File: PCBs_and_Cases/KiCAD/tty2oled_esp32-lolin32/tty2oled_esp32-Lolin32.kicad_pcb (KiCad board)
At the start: 2 copper layers, 35.6 x 99.7 mm, 12 parts

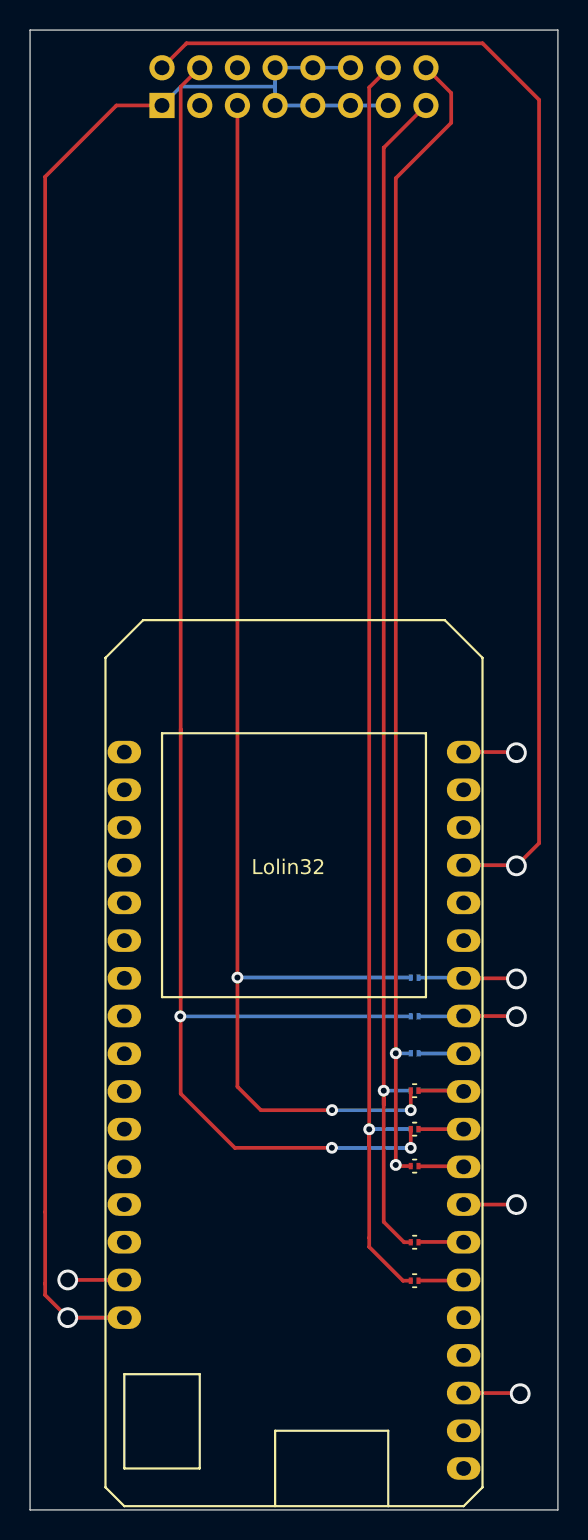
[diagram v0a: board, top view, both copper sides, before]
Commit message: Silkscreen fixed
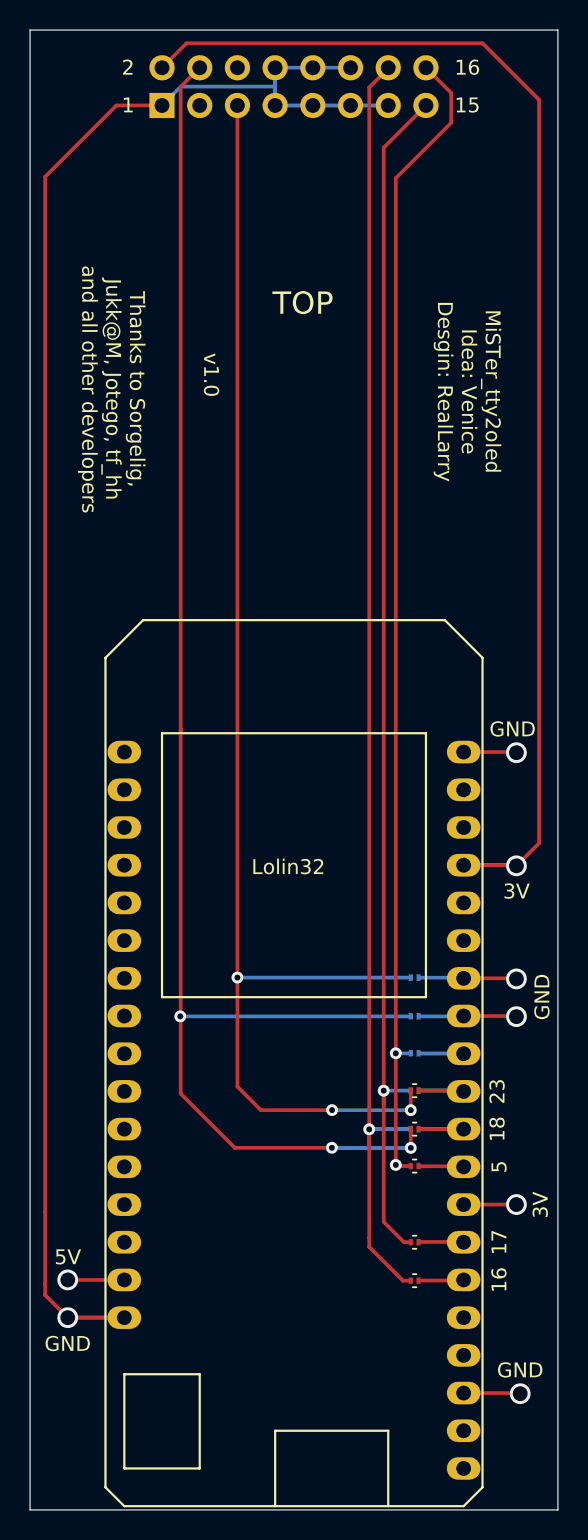
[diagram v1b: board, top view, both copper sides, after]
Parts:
- removed the REF** at (158.0, 122.9) (x2)
- added REF**: R_0201, Resistors_SMD:R_0201, B.Cu at (158.0, 122.9)
- added REF**: R_0201, Resistors_SMD:R_0201, F.Cu at (158.0, 122.9)
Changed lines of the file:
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@@
     )
   )
-  (gr_text v1.0 (at 144.272 74.676 -90) (layer F.Paste)
+  (gr_text v1.0 (at 144.272 74.676 -90) (layer F.SilkS)
     (effects (font (size 1 1) (thickness 0.15)))
   )
-  (gr_text "Thanks to Sorgelig,\nJukk@M, Jotego, tf_hh\nand all other developers" (at 137.668 75.6412 -90) (layer F.Paste)
+  (gr_text "Thanks to Sorgelig,\nJukk@M, Jotego, tf_hh\nand all other developers" (at 137.668 75.6412 -90) (layer F.SilkS)
     (effects (font (size 1 1) (thickness 0.15)))
   )
-  (gr_text "MiSTer_tty2oled\nIdea: Venice\nDesgin: RealLarry" (at 161.6329 75.7809 -90) (layer F.Paste)
+  (gr_text "MiSTer_tty2oled\nIdea: Venice\nDesgin: RealLarry" (at 161.6329 75.7809 -90) (layer F.SilkS)
     (effects (font (size 1 1) (thickness 0.15)))
   )
-  (gr_text 3V (at 166.4843 130.5941 90) (layer F.Paste)
+  (gr_text 3V (at 166.4843 130.5941 90) (layer F.SilkS)
     (effects (font (size 1 1) (thickness 0.15)))
   )
-  (gr_text 3V (at 164.846 109.474) (layer B.Paste)
+  (gr_text 3V (at 164.846 109.474) (layer B.SilkS)
     (effects (font (size 1 1) (thickness 0.15)) (justify mirror))
   )
-  (gr_text GND (at 134.62 139.954) (layer B.Paste)
+  (gr_text GND (at 134.62 139.954) (layer B.SilkS)
     (effects (font (size 1 1) (thickness 0.15)) (justify mirror))
   )
-  (gr_text 3V (at 164.846 109.474) (layer F.Paste)
+  (gr_text 3V (at 164.846 109.474) (layer F.SilkS)
     (effects (font (size 1 1) (thickness 0.15)))
   )
-  (gr_text GND (at 164.592 98.552) (layer F.Paste)
+  (gr_text GND (at 164.592 98.552) (layer F.SilkS)
     (effects (font (size 1 1) (thickness 0.15)))
   )
-  (gr_text GND (at 166.5986 116.5733 90) (layer F.Paste)
+  (gr_text GND (at 166.5986 116.5733 90) (layer F.SilkS)
     (effects (font (size 1 1) (thickness 0.15)))
   )
-  (gr_text GND (at 165.1 141.732) (layer F.Paste)
+  (gr_text GND (at 165.1 141.732) (layer F.SilkS)
     (effects (font (size 1 1) (thickness 0.15)))
   )
-  (gr_text GND (at 134.62 139.954) (layer F.Paste)
+  (gr_text GND (at 134.62 139.954) (layer F.SilkS)
     (effects (font (size 1 1) (thickness 0.15)))
   )
-  (gr_text 5V (at 134.62 134.112) (layer F.Paste)
+  (gr_text 5V (at 134.62 134.112) (layer F.SilkS)
     (effects (font (size 1 1) (thickness 0.15)))
   )
   (gr_line (start 167.64 51.435) (end 132.08 51.435) (layer Edge.Cuts) (width 0.05))
-  (gr_text BOT (at 150.5077 69.7992) (layer B.Paste)
+  (gr_text BOT (at 150.5077 69.7992) (layer B.SilkS)
     (effects (font (size 1.5 1.5) (thickness 0.3)) (justify mirror))
   )
-  (gr_text TOP (at 150.4696 69.85) (layer F.Paste)
+  (gr_text TOP (at 150.4696 69.85) (layer F.SilkS)
     (effects (font (size 1.5 1.5) (thickness 0.3)))
   )
-  (gr_text 16 (at 163.449 125.476 90) (layer B.Paste)
+  (gr_text 16 (at 163.449 125.476 90) (layer B.SilkS)
     (effects (font (size 1 1) (thickness 0.15)) (justify mirror))
   )
-  (gr_text 17 (at 163.449 122.936 90) (layer B.Paste)
+  (gr_text 17 (at 163.449 122.936 90) (layer B.SilkS)
     (effects (font (size 1 1) (thickness 0.15)) (justify mirror))
   )
-  (gr_text 16 (at 163.703 135.636 90) (layer F.Paste)
+  (gr_text 16 (at 163.703 135.636 90) (layer F.SilkS)
     (effects (font (size 1 1) (thickness 0.15)))
   )
-  (gr_text 17 (at 163.703 133.096 90) (layer F.Paste)
+  (gr_text 17 (at 163.703 133.096 90) (layer F.SilkS)
     (effects (font (size 1 1) (thickness 0.15)))
   )
-  (gr_text 5 (at 163.703 128.016 90) (layer F.Paste)
+  (gr_text 5 (at 163.703 128.016 90) (layer F.SilkS)
     (effects (font (size 1 1) (thickness 0.15)))
   )
-  (gr_text 18 (at 163.576 125.476 90) (layer F.Paste)
+  (gr_text 18 (at 163.576 125.476 90) (layer F.SilkS)
     (effects (font (size 1 1) (thickness 0.15)))
   )
-  (gr_text 23 (at 163.576 122.936 90) (layer F.Paste)
+  (gr_text 23 (at 163.576 122.936 90) (layer F.SilkS)
     (effects (font (size 1 1) (thickness 0.15)))
   )
-  (gr_text 5 (at 163.449 120.269 90) (layer B.Paste)
+  (gr_text 5 (at 163.449 120.269 90) (layer B.SilkS)
     (effects (font (size 1 1) (thickness 0.15)) (justify mirror))
   )
-  (gr_text 18 (at 163.449 117.856 90) (layer B.Paste)
+  (gr_text 18 (at 163.449 117.856 90) (layer B.SilkS)
     (effects (font (size 1 1) (thickness 0.15)) (justify mirror))
   )
-  (gr_text 23 (at 163.449 115.316 90) (layer B.Paste)
+  (gr_text 23 (at 163.449 115.316 90) (layer B.SilkS)
     (effects (font (size 1 1) (thickness 0.15)) (justify mirror))
   )
-  (gr_text 2 (at 138.684 53.975) (layer F.Paste)
+  (gr_text 2 (at 138.684 53.975) (layer F.SilkS)
     (effects (font (size 1 1) (thickness 0.15)))
   )
-  (gr_text 1 (at 138.684 56.515) (layer F.Paste)
+  (gr_text 1 (at 138.684 56.515) (layer F.SilkS)
     (effects (font (size 1 1) (thickness 0.15)))
   )
@@
   (gr_line (start 132.08 151.13) (end 167.64 151.13) (layer Edge.Cuts) (width 0.05))
   (target plus (at 132.08 151.13) (size 5) (width 0.05) (layer Edge.Cuts))
-  (gr_text 16 (at 161.544 53.975) (layer F.Paste)
+  (gr_text 16 (at 161.544 53.975) (layer F.SilkS)
     (effects (font (size 1 1) (thickness 0.15)))
   )
-  (gr_text 15 (at 161.544 56.515) (layer F.Paste)
+  (gr_text 15 (at 161.544 56.515) (layer F.SilkS)
     (effects (font (size 1 1) (thickness 0.15)))
   )

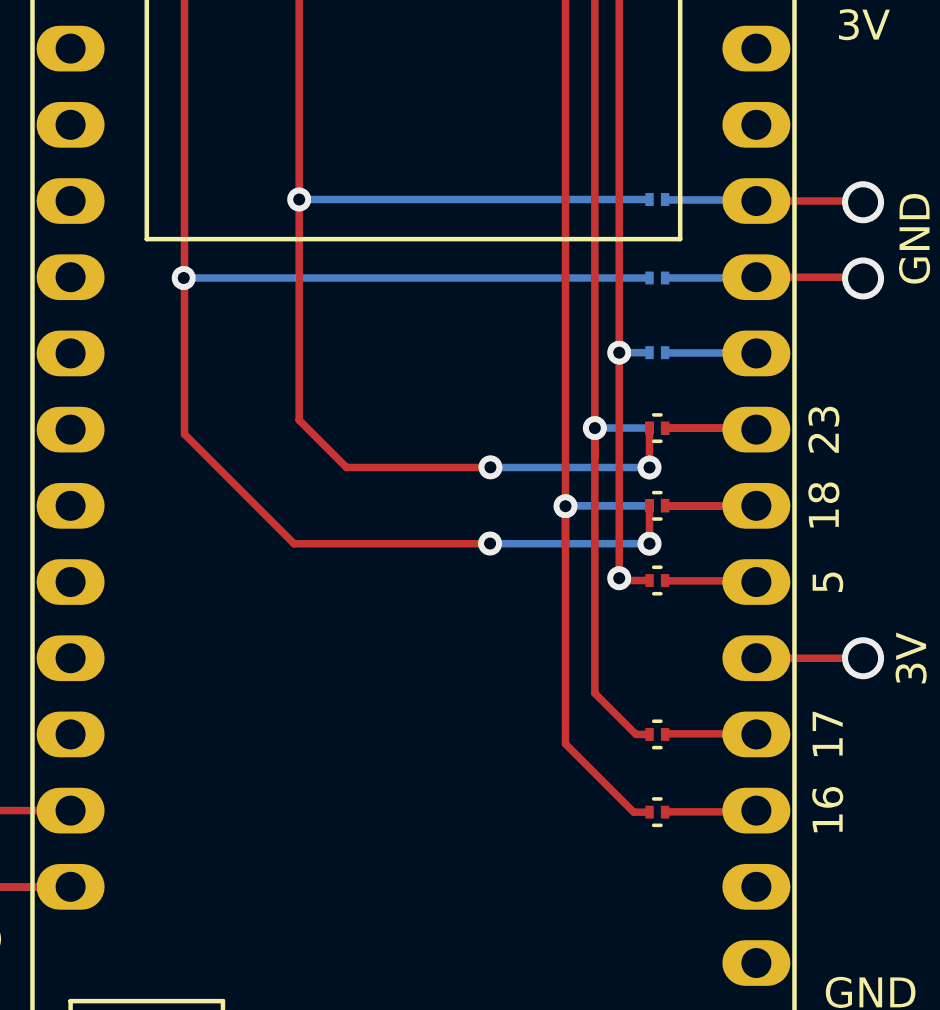
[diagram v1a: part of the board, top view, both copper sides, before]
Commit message: Rework of Lolin32 PCB. 0201 Pads were a bad idea.
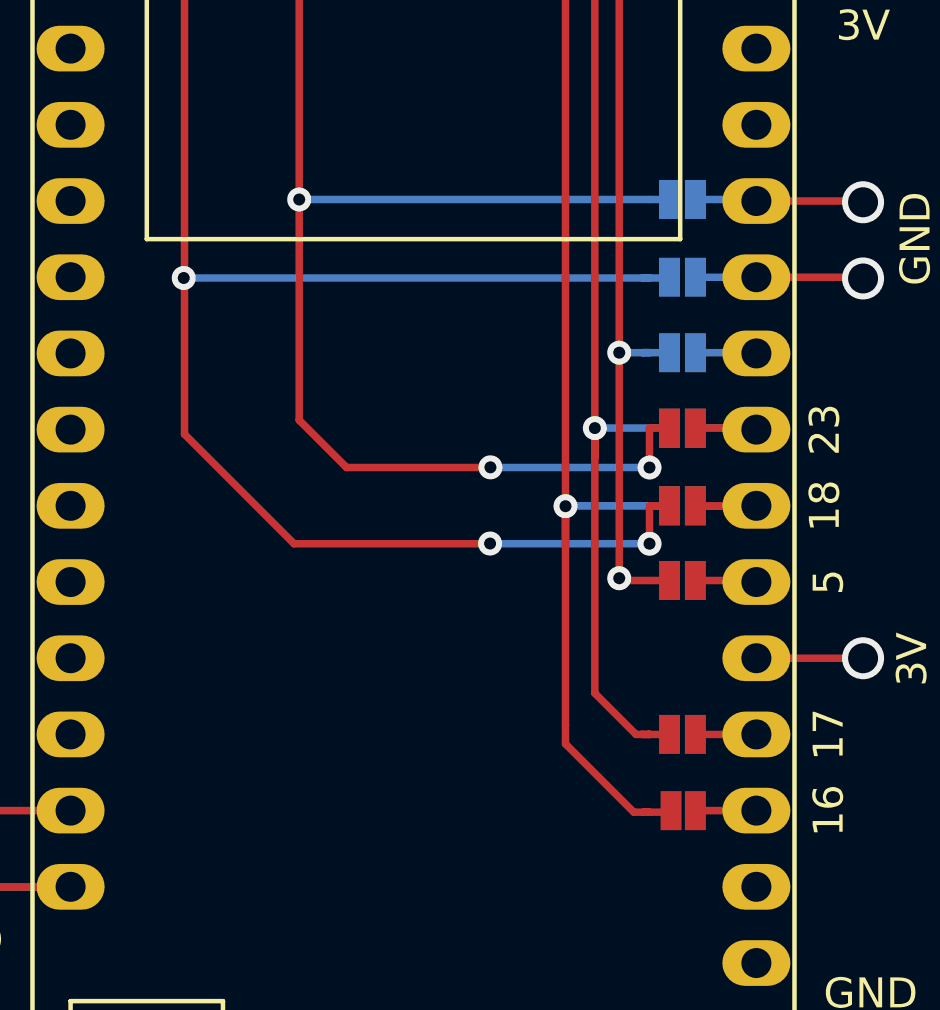
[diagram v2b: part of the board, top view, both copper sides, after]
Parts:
- removed the REF** at (158.0, 115.3)
- removed the REF** at (158.0, 135.7)
- removed the REF** at (158.0, 117.9)
- removed the REF** at (158.0, 120.4)
- removed the REF** at (158.0, 122.9) (x2)
- removed the REF** at (158.0, 125.5)
- removed the REF** at (158.0, 128.0)
- removed the REF** at (158.0, 133.1)
- added REF**: PADS_0805, _my_footprints:PAD_0805, B.Cu at (158.8, 122.9)
- added REF**: PADS_0805, _my_footprints:PAD_0805, F.Cu at (158.9, 135.6)
- added REF**: PADS_0805, _my_footprints:PAD_0805, B.Cu at (158.8, 115.3)
- added REF**: PADS_0805, _my_footprints:PAD_0805, B.Cu at (158.8, 120.4)
- added REF**: PADS_0805, _my_footprints:PAD_0805, B.Cu at (158.8, 117.9)
- added REF**: PADS_0805, _my_footprints:PAD_0805, F.Cu at (158.8, 122.9)
- added REF**: PADS_0805, _my_footprints:PAD_0805, F.Cu at (158.8, 125.5)
- added REF**: PADS_0805, _my_footprints:PAD_0805, F.Cu at (158.8, 128.0)
- added REF**: PADS_0805, _my_footprints:PAD_0805, F.Cu at (158.8, 133.1)
- REF**: value R_0201 -> PADS_0805; footprint Resistors_SMD:R_0201 -> _my_footprints:PAD_0805
- moved REF** 0.84 mm to (158.8, 125.5)
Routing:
- net (no net): track 701.7 -> 699.9 mm

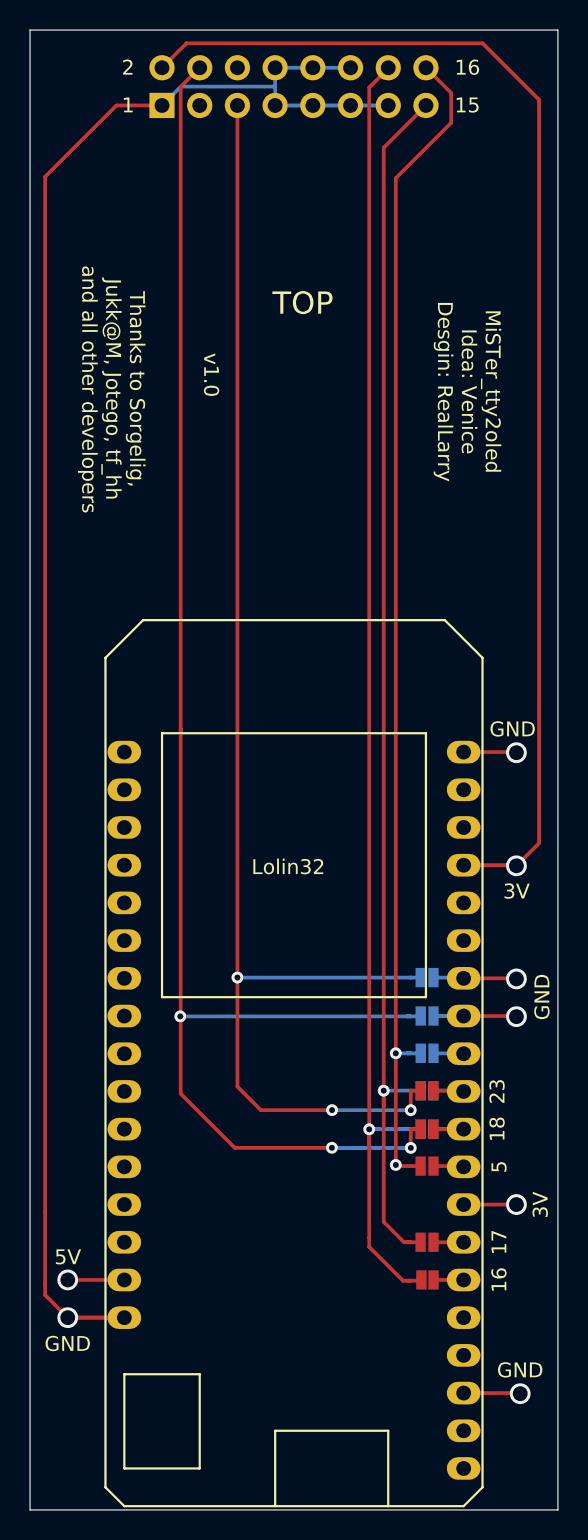
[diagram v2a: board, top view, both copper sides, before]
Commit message: Update board esp32-lolin32 to v1.1
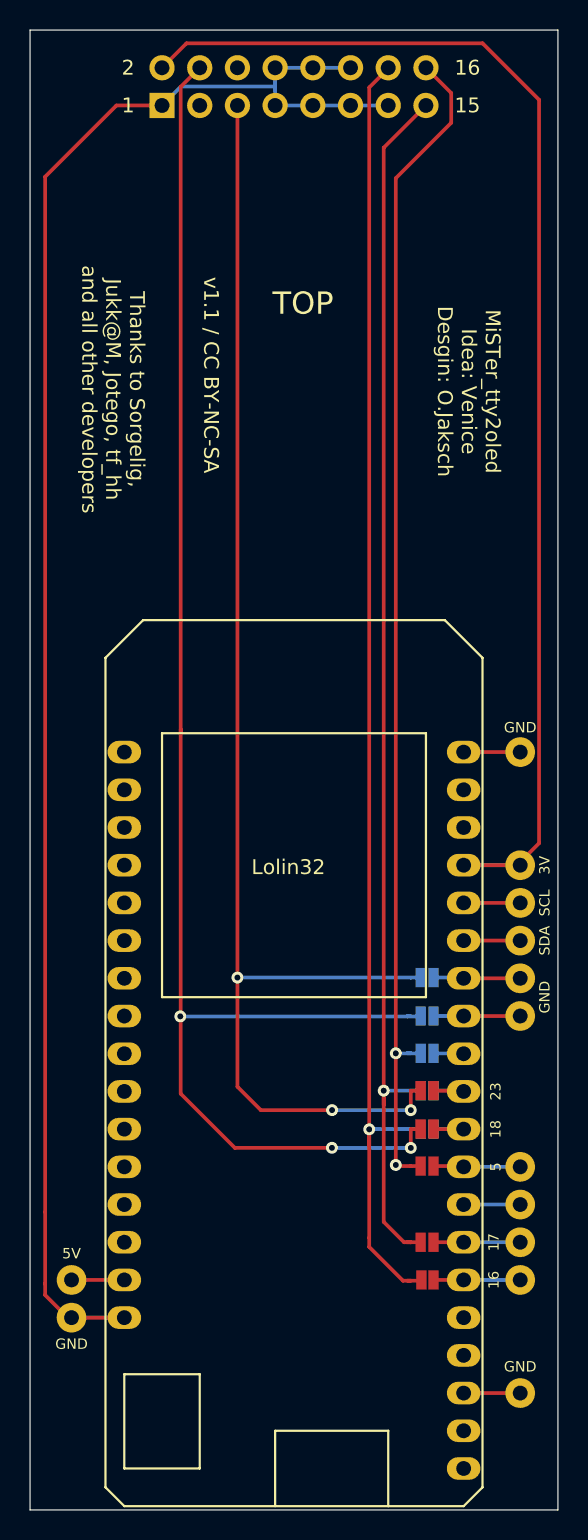
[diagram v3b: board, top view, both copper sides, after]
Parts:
- removed the REF** at (158.8, 122.9) (x2)
- added REF**: SolderWirePad_single_0-8mmDrill, Wire_Pads:SolderWirePad_single_0-8mmDrill, F.Cu at (165.1, 143.3)
- added REF**: SolderWirePad_single_0-8mmDrill, Wire_Pads:SolderWirePad_single_0-8mmDrill, F.Cu at (165.1, 110.2)
- added REF**: SolderWirePad_single_0-8mmDrill, Wire_Pads:SolderWirePad_single_0-8mmDrill, F.Cu at (165.1, 112.8)
- added REF**: SolderWirePad_single_0-8mmDrill, Wire_Pads:SolderWirePad_single_0-8mmDrill, F.Cu at (165.1, 117.9)
- added REF**: SolderWirePad_single_0-8mmDrill, Wire_Pads:SolderWirePad_single_0-8mmDrill, F.Cu at (165.1, 115.3)
- added REF**: PADS_0805, _my_footprints:PAD_0805, B.Cu at (158.8, 122.9)
- added REF**: PADS_0805, _my_footprints:PAD_0805, F.Cu at (158.8, 122.9)
- added REF**: SolderWirePad_single_0-8mmDrill, Wire_Pads:SolderWirePad_single_0-8mmDrill, F.Cu at (165.1, 128.0)
- added REF**: SolderWirePad_single_0-8mmDrill, Wire_Pads:SolderWirePad_single_0-8mmDrill, F.Cu at (165.1, 130.6)
- added REF**: SolderWirePad_single_0-8mmDrill, Wire_Pads:SolderWirePad_single_0-8mmDrill, F.Cu at (165.1, 133.1)
- added REF**: SolderWirePad_single_0-8mmDrill, Wire_Pads:SolderWirePad_single_0-8mmDrill, F.Cu at (165.1, 135.6)
- added REF**: SolderWirePad_single_0-8mmDrill, Wire_Pads:SolderWirePad_single_0-8mmDrill, F.Cu at (134.9, 138.2)
- added REF**: SolderWirePad_single_0-8mmDrill, Wire_Pads:SolderWirePad_single_0-8mmDrill, F.Cu at (134.9, 135.6)
- added REF**: SolderWirePad_single_0-8mmDrill, Wire_Pads:SolderWirePad_single_0-8mmDrill, F.Cu at (165.1, 107.7)
- added REF**: SolderWirePad_single_0-8mmDrill, Wire_Pads:SolderWirePad_single_0-8mmDrill, F.Cu at (165.1, 100.1)
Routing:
- net (no net): track 699.9 -> 717.3 mm, vias 18 -> 10
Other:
- board text added: "MiSTer_tty2oled Idea: Venice Desgin: O.Jaksch"
- board text added: "SCL"
- board text added: "SCL1"
- board text added: "SCL2"
- board text added: "SDA"
- board text added: "SDA1"
- board text added: "SDA2"
- board text added: "v1.1 / CC BY-NC-SA"
- board text removed: "MiSTer_tty2oled Idea: Venice Desgin: RealLarry"
- board text removed: "v1.0"
